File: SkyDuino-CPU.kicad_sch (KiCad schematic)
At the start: 39 parts, among them J11 DBG, J12 USB-A RMT, J13 DISP, J14 USB_C Artisan, SW1 BOOT, U10 USBLC6-2SC6, U7 25MHz, U8 USBLC6-2SC6, U9 STM32F411RET6, Y1 32.768kHz

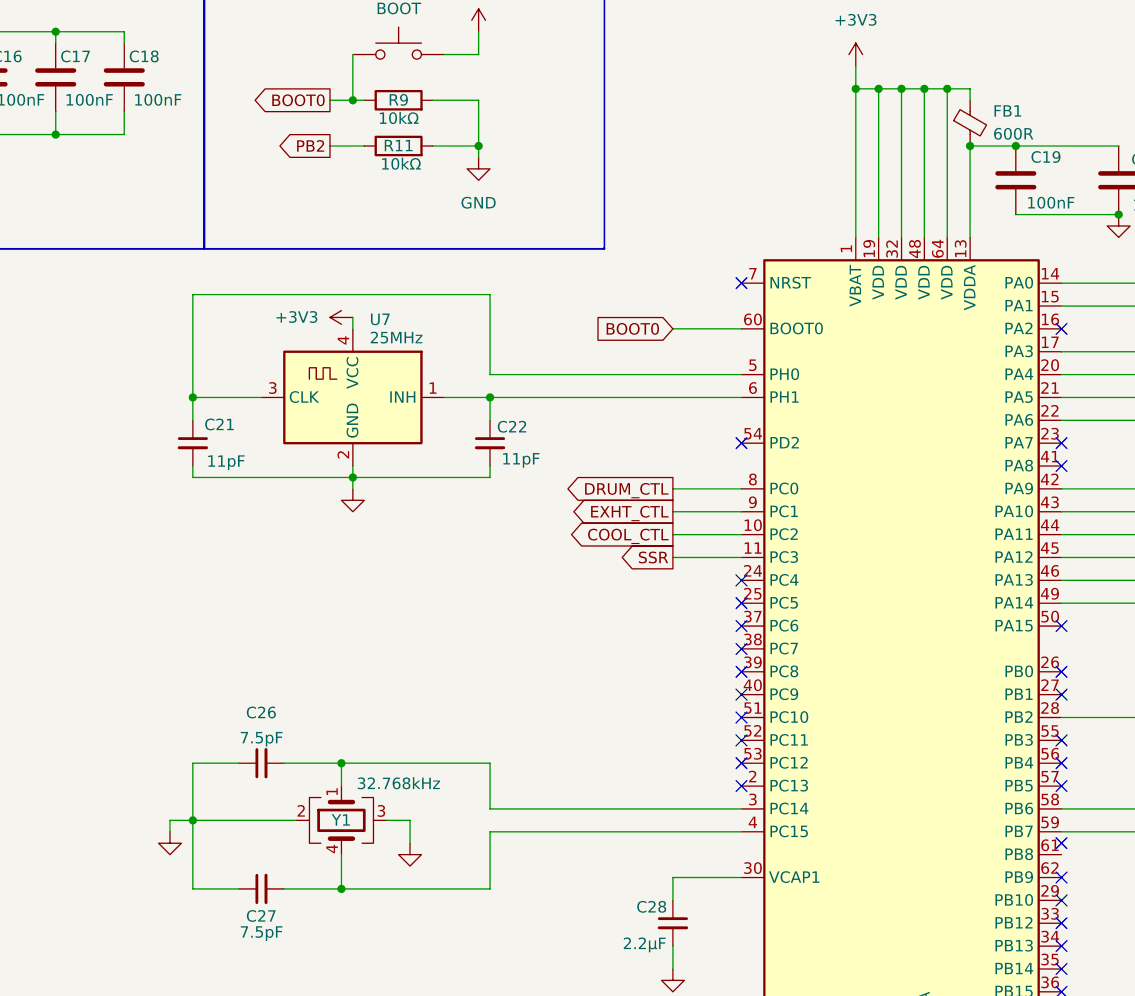
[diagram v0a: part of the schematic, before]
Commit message: Rearrange components. Fix 25MHz oscillator connection
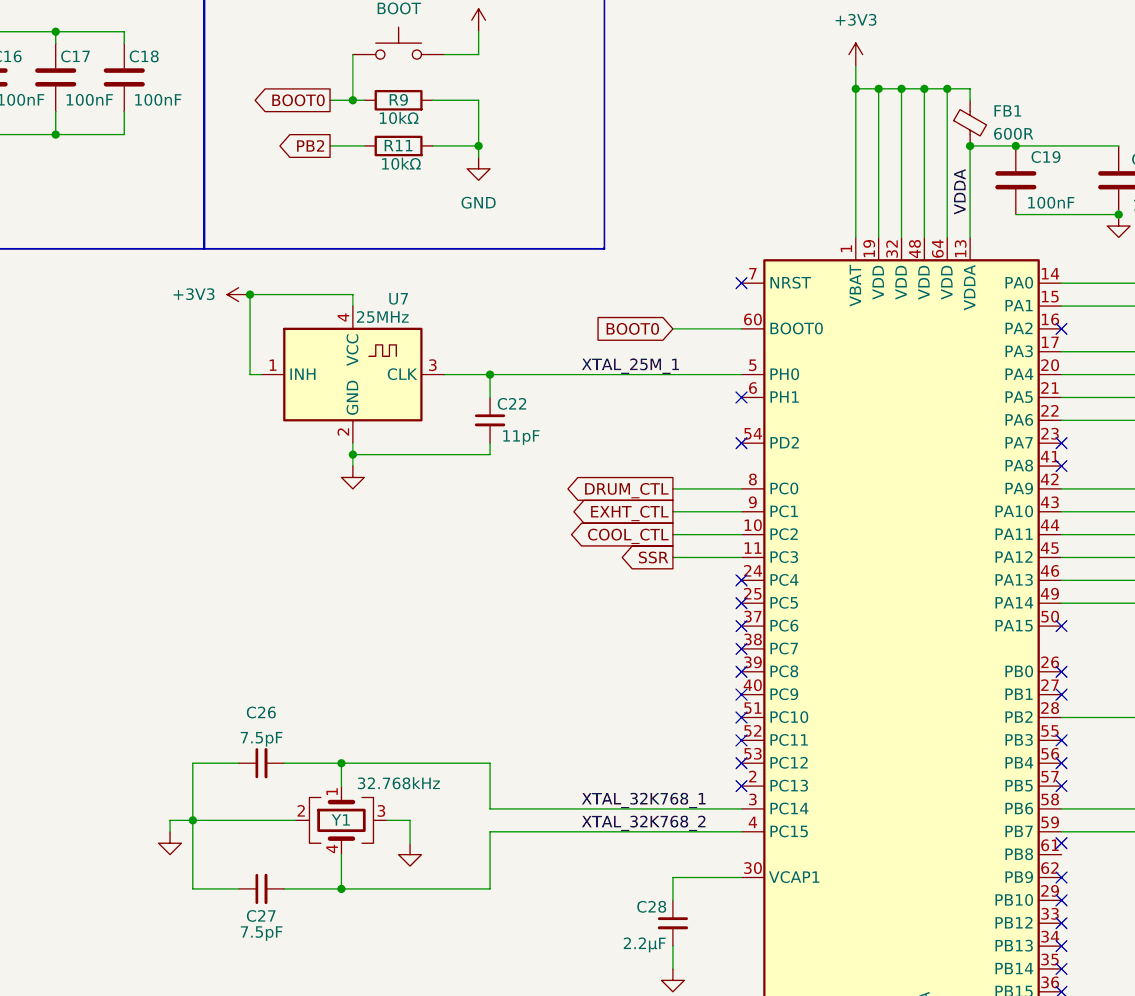
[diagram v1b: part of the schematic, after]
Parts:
- removed C21: 11pF, Capacitor_SMD:C_0805_2012Metric_Pad1.18x1.45mm_HandSolder, symbol Device:C_Small
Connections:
- net +3V3: now also U7.1 (INH)
- net VDDA: now reaches C19.2, C20.2, FB1.2, U9.13 (VDDA)
- net XTAL_32K768_1: now reaches C26.2, U9.3 (PC14), Y1.1
- net XTAL_32K768_2: now reaches C27.2, U9.4 (PC15), Y1.4
- net XTAL_25M_1: now reaches U7.3 (CLK), U9.5 (PH0)
- net XTAL_25M_1: now also C22.1
- now unconnected: U9.6 (PH1)
- no-connect marks 29 -> 30
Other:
- moved on the sheet: C22, U7

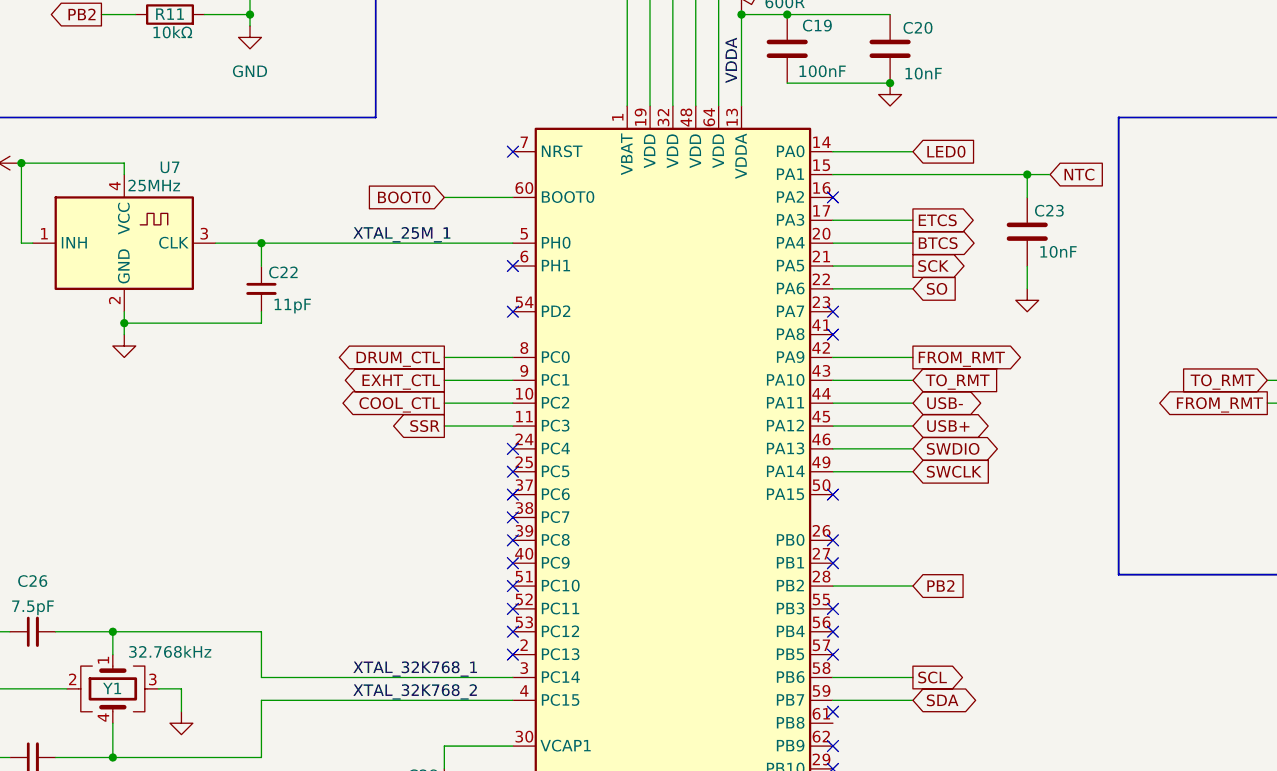
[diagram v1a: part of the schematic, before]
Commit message: Optimize pinouts
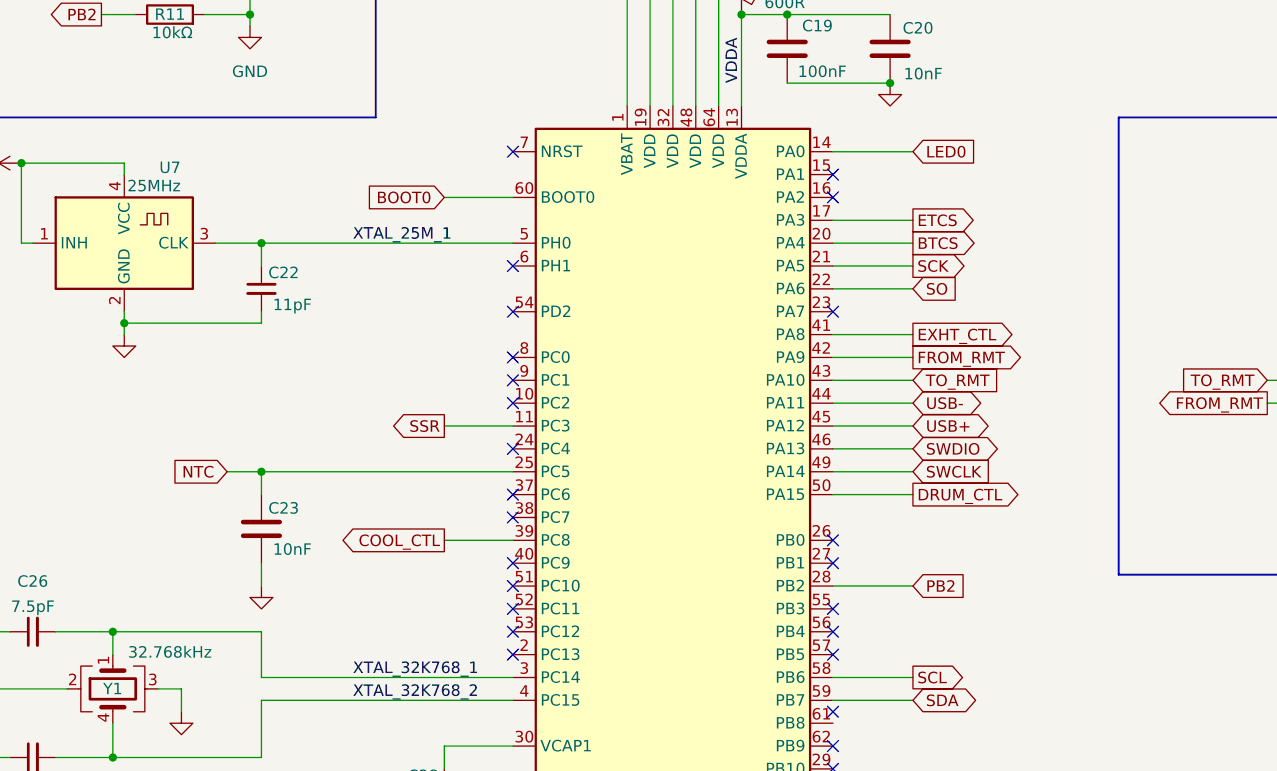
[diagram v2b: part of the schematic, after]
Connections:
- net COOL_CTL: now also U9.39 (PC8); no longer U9.10 (PC2)
- net DRUM_CTL: now also U9.50 (PA15); no longer U9.8 (PC0)
- net EXHT_CTL: now also U9.41 (PA8); no longer U9.9 (PC1)
- net NTC: now also U9.25 (PC5); no longer U9.15 (PA1)
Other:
- moved on the sheet: C23
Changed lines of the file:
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@@
 	)
 	(junction
+		(at 107.95 87.63)
+		(diameter 0)
+		(color 0 0 0 0)
+	)
+	(junction
 		(at 91.44 105.41)
 		(diameter 0)
@@
 		(color 0 0 0 0)
 	)
-	(junction
-		(at 193.04 54.61)
-		(diameter 0)
-		(color 0 0 0 0)
-	)
 	(no_connect
-		(at 135.89 97.79)
+		(at 135.89 80.01)
 	)
 	(no_connect
@@
 	)
 	(no_connect
-		(at 171.45 90.17)
+		(at 135.89 74.93)
 	)
 	(no_connect
@@
 	)
 	(no_connect
-		(at 135.89 95.25)
+		(at 135.89 97.79)
 	)
 	(no_connect
@@
 	)
 	(no_connect
-		(at 135.89 87.63)
+		(at 171.45 54.61)
 	)
 	(no_connect
@@
 	)
 	(no_connect
-		(at 171.45 72.39)
+		(at 135.89 77.47)
 	)
 	(no_connect
@@
 	(wire
 		(pts
-			(xy 128.27 74.93) (xy 135.89 74.93)
+			(xy 180.34 90.17) (xy 171.45 90.17)
 		)
 		(stroke
@@
 	(wire
 		(pts
-			(xy 128.27 77.47) (xy 135.89 77.47)
+			(xy 180.34 72.39) (xy 171.45 72.39)
 		)
 		(stroke
@@
 	(wire
 		(pts
-			(xy 128.27 80.01) (xy 135.89 80.01)
+			(xy 128.27 95.25) (xy 135.89 95.25)
 		)
 		(stroke
@@
 	(wire
 		(pts
+			(xy 107.95 87.63) (xy 135.89 87.63)
+		)
+		(stroke
+			(width 0)
+			(type default)
+		)
+	)
+	(wire
+		(pts
 			(xy 156.21 30.48) (xy 153.67 30.48)
 		)
@@
 	(wire
 		(pts
-			(xy 193.04 57.15) (xy 193.04 54.61)
+			(xy 107.95 90.17) (xy 107.95 87.63)
 		)
 		(stroke
@@
 	(wire
 		(pts
+			(xy 107.95 97.79) (xy 107.95 100.33)
+		)
+		(stroke
+			(width 0)
+			(type default)
+		)
+	)
+	(wire
+		(pts
 			(xy 25.4 24.13) (xy 25.4 25.4)
 		)
@@
 	(wire
 		(pts
-			(xy 34.29 33.02) (xy 34.29 35.56)
+			(xy 104.14 87.63) (xy 107.95 87.63)
 		)
 		(stroke
@@
 	(wire
 		(pts
-			(xy 135.89 62.23) (xy 107.95 62.23)
+			(xy 34.29 33.02) (xy 34.29 35.56)
 		)
 		(stroke
@@
 	(wire
 		(pts
-			(xy 54.61 147.32) (xy 55.88 147.32)
+			(xy 135.89 62.23) (xy 107.95 62.23)
 		)
 		(stroke
@@
 	(wire
 		(pts
-			(xy 171.45 113.03) (xy 180.34 113.03)
+			(xy 54.61 147.32) (xy 55.88 147.32)
 		)
 		(stroke
@@
 	(wire
 		(pts
-			(xy 30.48 180.34) (xy 30.48 189.23)
+			(xy 171.45 113.03) (xy 180.34 113.03)
 		)
 		(stroke
@@
 	(wire
 		(pts
-			(xy 171.45 67.31) (xy 180.34 67.31)
+			(xy 30.48 180.34) (xy 30.48 189.23)
 		)
 		(stroke
@@
 	(wire
 		(pts
-			(xy 171.45 54.61) (xy 193.04 54.61)
+			(xy 171.45 67.31) (xy 180.34 67.31)
 		)
 		(stroke
@@
 	(wire
 		(pts
-			(xy 193.04 64.77) (xy 193.04 67.31)
-		)
-		(stroke
-			(width 0)
-			(type default)
-		)
-	)
-	(wire
-		(pts
 			(xy 59.69 24.13) (xy 67.31 24.13)
 		)
@@
 	(wire
 		(pts
-			(xy 193.04 54.61) (xy 195.58 54.61)
-		)
-		(stroke
-			(width 0)
-			(type default)
-		)
-	)
-	(wire
-		(pts
 			(xy 254 29.21) (xy 256.54 29.21)
 		)
@@
 	(global_label "EXHT_CTL"
 		(shape output)
-		(at 128.27 77.47 180)
+		(at 180.34 72.39 0)
 		(fields_autoplaced yes)
 		(effects
@@
 				(size 1.27 1.27)
 			)
-			(justify right)
+			(justify left)
 		)
 		(property "Intersheetrefs" "${INTERSHEET_REFS}"
-			(at 116.3949 77.47 0)
+			(at 192.2151 72.39 0)
 			(effects
 				(font
 					(size 1.27 1.27)
 				)
-				(justify right)
+				(justify left)
 				(hide yes)
 			)
@@
 	(global_label "DRUM_CTL"
 		(shape output)
-		(at 128.27 74.93 180)
+		(at 180.34 90.17 0)
 		(fields_autoplaced yes)
 		(effects
@@
 				(size 1.27 1.27)
 			)
-			(justify right)
+			(justify left)
 		)
 		(property "Intersheetrefs" "${INTERSHEET_REFS}"
-			(at 115.7296 74.93 0)
+			(at 192.8804 90.17 0)
 			(effects
 				(font
 					(size 1.27 1.27)
 				)
-				(justify right)
+				(justify left)
 				(hide yes)
 			)
@@
 	(global_label "NTC"
 		(shape input)
-		(at 195.58 54.61 0)
+		(at 104.14 87.63 180)
 		(fields_autoplaced yes)
 		(effects
@@
 				(size 1.27 1.27)
 			)
-			(justify left)
+			(justify right)
 		)
 		(property "Intersheetrefs" "${INTERSHEET_REFS}"
-			(at 202.1333 54.61 0)
+			(at 97.5867 87.63 0)
 			(effects
 				(font
 					(size 1.27 1.27)
 				)
-				(justify left)
+				(justify right)
 				(hide yes)
 			)
@@
 	(global_label "COOL_CTL"
 		(shape output)
-		(at 128.27 80.01 180)
+		(at 128.27 95.25 180)
 		(fields_autoplaced yes)
 		(effects
@@
 		)
 		(property "Intersheetrefs" "${INTERSHEET_REFS}"
-			(at 116.0924 80.01 0)
+			(at 116.0924 95.25 0)
 			(effects
 				(font
@@
 	(symbol
 		(lib_id "power:GND")
-		(at 193.04 67.31 0)
+		(at 107.95 100.33 0)
 		(unit 1)
 		(exclude_from_sim no)
@@
 		(fields_autoplaced yes)
 		(property "Reference" "#PWR01"
-			(at 193.04 73.66 0)
+			(at 107.95 106.68 0)
 			(effects
 				(font
@@
 		)
 		(property "Value" "GND"
-			(at 193.04 72.39 0)
+			(at 107.95 105.41 0)
 			(effects
 				(font
@@
 		)
 		(property "Footprint" ""
-			(at 193.04 67.31 0)
+			(at 107.95 100.33 0)
 			(effects
 				(font
@@
 		)
 		(property "Datasheet" ""
-			(at 193.04 67.31 0)
+			(at 107.95 100.33 0)
 			(effects
 				(font
@@
 		)
 		(property "Description" "Power symbol creates a global label with name \"GND\" , ground"
-			(at 193.04 67.31 0)
+			(at 107.95 100.33 0)
 			(effects
 				(font
@@
 	(symbol
 		(lib_id "Device:C")
-		(at 193.04 60.96 0)
+		(at 107.95 93.98 0)
 		(unit 1)
 		(exclude_from_sim no)
@@
 		(dnp no)
 		(property "Reference" "C23"
-			(at 193.802 58.674 0)
+			(at 108.712 91.694 0)
 			(effects
 				(font
@@
 		)
 		(property "Value" "10nF"
-			(at 194.31 63.246 0)
+			(at 109.22 96.266 0)
 			(effects
 				(font
@@
 		)
 		(property "Footprint" "Capacitor_SMD:C_0805_2012Metric_Pad1.18x1.45mm_HandSolder"
-			(at 194.0052 64.77 0)
+			(at 108.9152 97.79 0)
 			(effects
 				(font
@@
 		)
 		(property "Datasheet" "https://product.tdk.com/system/files/dam/doc/product/capacitor/ceramic/mlcc/catalog/mlcc_commercial_general_en.pdf?ref_disty=mouser"
-			(at 193.04 60.96 0)
+			(at 107.95 93.98 0)
 			(effects
 				(font
@@
 		)
 		(property "Description" "Unpolarized capacitor"
-			(at 193.04 60.96 0)
+			(at 107.95 93.98 0)
 			(effects
 				(font
@@
 		)
 		(property "Mouser pn" "810-C2012C0G1H103J-1"
-			(at 193.04 60.96 0)
+			(at 107.95 93.98 0)
 			(effects
 				(font
@@
 		)
 		(property "Mouser" "https://www.mouser.com/ProductDetail/TDK/C2012C0G1H103J060AA?qs=dfay7wIA1uESihXTlxZAiQ%3D%3D"
-			(at 193.04 60.96 0)
+			(at 107.95 93.98 0)
 			(effects
 				(font

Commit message: Remove 25MHz load cap
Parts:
- removed C22: 11pF, Capacitor_SMD:C_0805_2012Metric_Pad1.18x1.45mm_HandSolder, symbol Device:C_Small
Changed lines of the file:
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@@
 	)
 	(junction
-		(at 92.71 71.12)
-		(diameter 0)
-		(color 0 0 0 0)
-	)
-	(junction
 		(at 156.21 140.97)
 		(diameter 0)
@@
 	)
 	(junction
-		(at 107.95 62.23)
-		(diameter 0)
-		(color 0 0 0 0)
-	)
-	(junction
 		(at 260.35 57.15)
 		(diameter 0)
@@
 	(wire
 		(pts
-			(xy 92.71 71.12) (xy 92.71 72.39)
+			(xy 92.71 69.85) (xy 92.71 72.39)
 		)
 		(stroke
@@
 	(wire
 		(pts
-			(xy 92.71 69.85) (xy 92.71 71.12)
-		)
-		(stroke
-			(width 0)
-			(type default)
-		)
-	)
-	(wire
-		(pts
 			(xy 107.95 113.03) (xy 107.95 119.38)
 		)
@@
 	(wire
 		(pts
-			(xy 107.95 64.77) (xy 107.95 62.23)
-		)
-		(stroke
-			(width 0)
-			(type default)
-		)
-	)
-	(wire
-		(pts
 			(xy 48.26 154.94) (xy 48.26 157.48)
 		)
@@
 	(wire
 		(pts
-			(xy 107.95 71.12) (xy 92.71 71.12)
-		)
-		(stroke
-			(width 0)
-			(type default)
-		)
-	)
-	(wire
-		(pts
 			(xy 17.78 35.56) (xy 17.78 38.1)
 		)
@@
 	(wire
 		(pts
-			(xy 107.95 69.85) (xy 107.95 71.12)
-		)
-		(stroke
-			(width 0)
-			(type default)
-		)
-	)
-	(wire
-		(pts
 			(xy 85.09 119.38) (xy 91.44 119.38)
 		)
@@
 	(wire
 		(pts
-			(xy 107.95 62.23) (xy 102.87 62.23)
-		)
-		(stroke
-			(width 0)
-			(type default)
-		)
-	)
-	(wire
-		(pts
 			(xy 251.46 57.15) (xy 260.35 57.15)
 		)
@@
 	(wire
 		(pts
-			(xy 135.89 62.23) (xy 107.95 62.23)
+			(xy 102.87 62.23) (xy 135.89 62.23)
 		)
 		(stroke
@@
 					(unit 1)
 				)
-			)
-		)
-	)
-	(symbol
-		(lib_id "Device:C_Small")
-		(at 107.95 67.31 0)
-		(unit 1)
-		(exclude_from_sim no)
-		(in_bom yes)
-		(on_board yes)
-		(dnp no)
-		(property "Reference" "C22"
-			(at 108.712 65.532 0)
-			(effects
-				(font
-					(size 1.27 1.27)
-				)
-				(justify left)
-			)
-		)
-		(property "Value" "11pF	"
-			(at 109.22 69.088 0)
-			(effects
-				(font
-					(size 1.27 1.27)
-				)
-				(justify left)
-			)
-		)
-		(property "Footprint" "Capacitor_SMD:C_0805_2012Metric_Pad1.18x1.45mm_HandSolder"
-			(at 107.95 67.31 0)
-			(effects
-				(font
-					(size 1.27 1.27)
-				)
-				(hide yes)
-			)
-		)
-		(property "Datasheet" "https://www.mouser.com/datasheet/2/40/C0GNP0_Dielectric-2952720.pdf"
-			(at 107.95 67.31 0)
-			(effects
-				(font
-					(size 1.27 1.27)
-				)
-				(hide yes)
-			)
-		)
-		(property "Description" "Unpolarized capacitor, small symbol"
-			(at 107.95 67.31 0)
-			(effects
-				(font
-					(size 1.27 1.27)
-				)
-				(hide yes)
-			)
-		)
-		(property "Mouser pn" "581-08055A110JAT2A"
-			(at 107.95 67.31 0)
-			(effects
-				(font
-					(size 1.27 1.27)
-				)
-				(hide yes)
-			)
-		)
-		(pin "1"
-		)
-		(pin "2"
-		)
-		(instances
-			(project "SkyDuino-Hardware"
-				(path "/a6671232-96de-4e23-ad68-f9378c1c0159/30f0c390-a08b-495d-a987-fe20b2c7c730"
-					(reference "C22")
-					(unit 1)
-				)

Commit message: Optimize SSR pin
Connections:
- net SSR: now also U9.62 (PB9); no longer U9.11 (PC3)
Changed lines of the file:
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@@
 	)
 	(no_connect
-		(at 171.45 114.3)
+		(at 171.45 115.57)
 	)
 	(no_connect
@@
 	)
 	(no_connect
-		(at 171.45 118.11)
+		(at 135.89 82.55)
 	)
 	(no_connect
@@
 	(wire
 		(pts
-			(xy 128.27 82.55) (xy 135.89 82.55)
+			(xy 180.34 118.11) (xy 171.45 118.11)
 		)
 		(stroke
@@
 	(global_label "SSR"
 		(shape output)
-		(at 128.27 82.55 180)
+		(at 180.34 118.11 0)
 		(fields_autoplaced yes)
 		(effects
@@
 				(size 1.27 1.27)
 			)
-			(justify right)
+			(justify left)
 		)
 		(property "Intersheetrefs" "${INTERSHEET_REFS}"
-			(at 121.5958 82.55 0)
+			(at 187.0142 118.11 0)
 			(effects
 				(font
 					(size 1.27 1.27)
 				)
-				(justify right)
+				(justify left)
 				(hide yes)
 			)

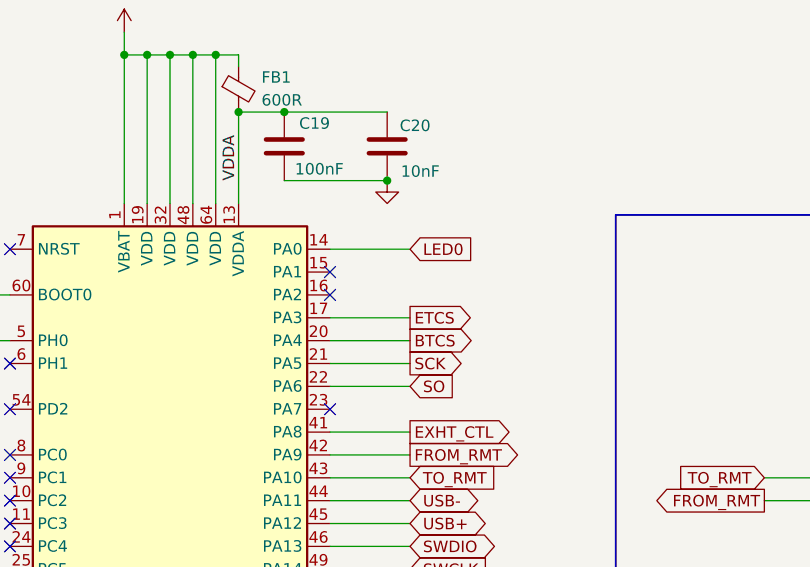
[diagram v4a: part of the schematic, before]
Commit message: Optimize LED pin
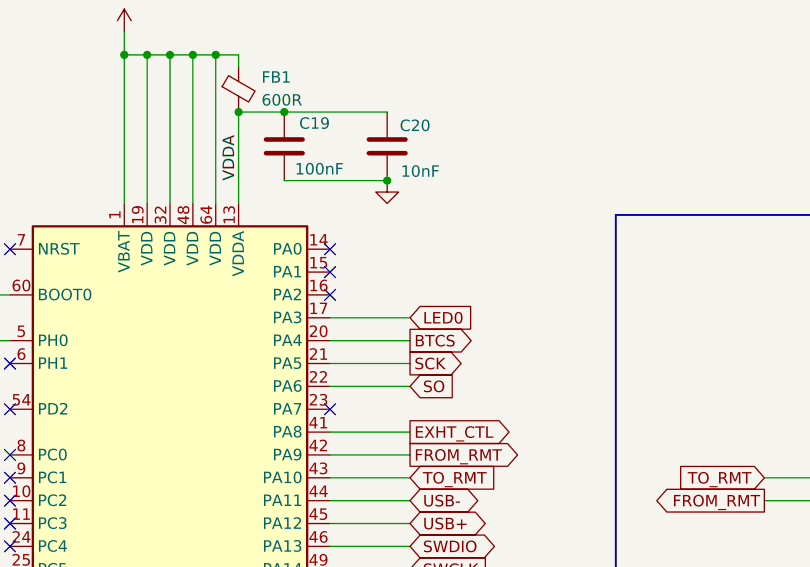
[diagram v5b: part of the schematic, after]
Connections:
- net ETCS is gone; now on net LED0: U9.17 (PA3)
- net LED0: no longer U9.14 (PA0)
- no-connect marks 30 -> 31
